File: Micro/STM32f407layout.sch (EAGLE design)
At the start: 68 parts, among them Q1 ASF, Q2 ASV-8, T3 FDN340P, T4 AP1117_LIN_REG

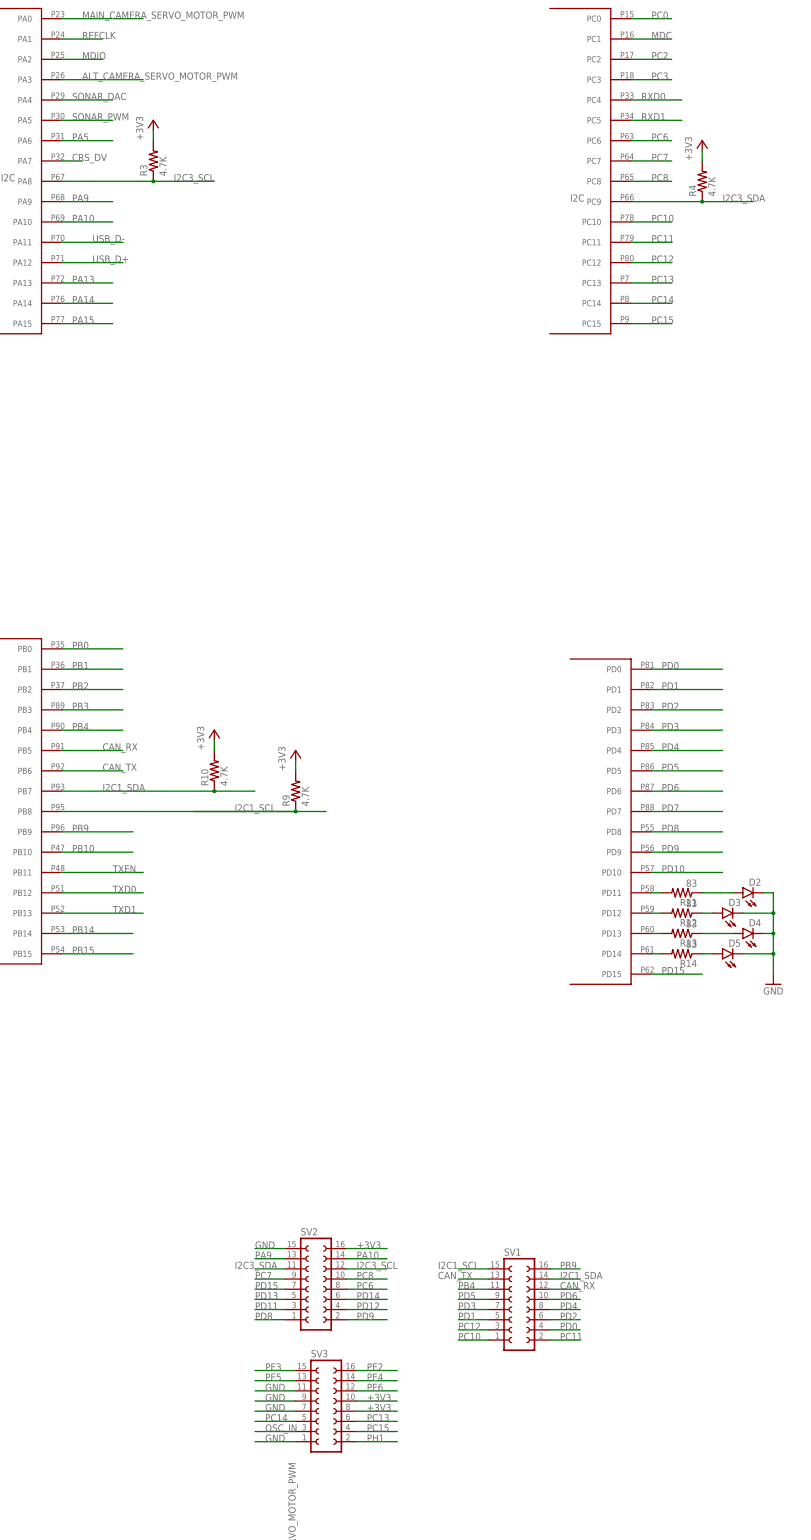
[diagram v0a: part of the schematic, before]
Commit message: Added rough sketch for bottom pinout
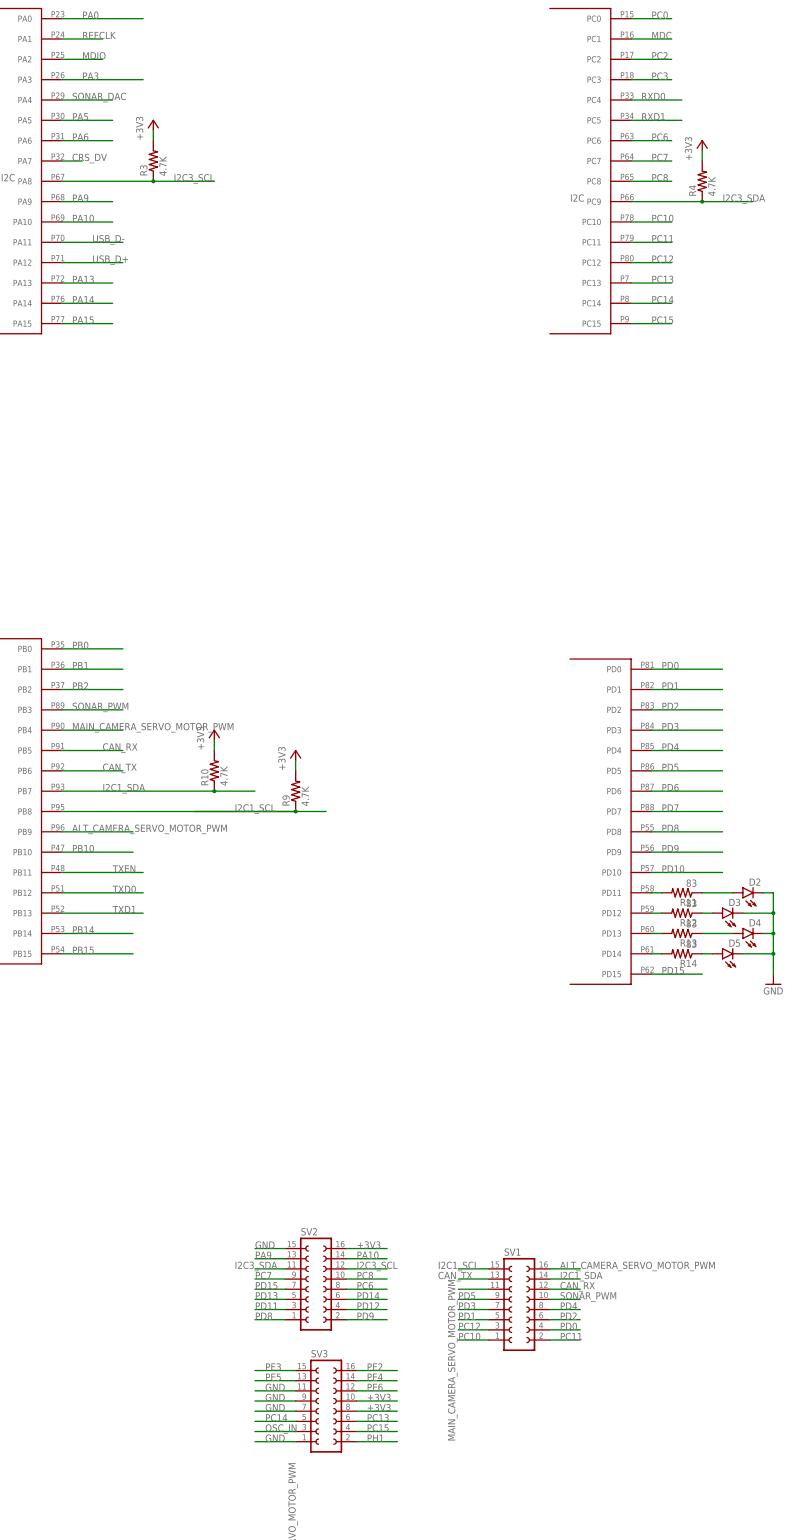
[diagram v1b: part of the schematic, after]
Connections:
- removed net PB3: U$1G$2.PB3
- removed net PB4: SV1.11, U$1G$2.PB4
- removed net PB9: SV1.16, U$1G$2.PB9
- new net PA0: U$1G$1.PA0
- new net PA3: U$1G$1.PA3
- new net PA6: U$1G$1.PA6
- net ALT_CAMERA_SERVO_MOTOR_PWM: now also SV1.16, U$1G$2.PB9; no longer U$1G$1.PA3
- net MAIN_CAMERA_SERVO_MOTOR_PWM: now also SV1.11, U$1G$2.PB4; no longer U$1G$1.PA0
- net PA5: now also U$1G$1.PA5; no longer U$1G$1.PA6
- net PD6: no longer SV1.10
- net SONAR_PWM: now also SV1.10, U$1G$2.PB3; no longer U$1G$1.PA5
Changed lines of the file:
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@@
 <?xml version="1.0" encoding="utf-8"?>
 <!DOCTYPE eagle SYSTEM "eagle.dtd">
-<eagle version="7.4.0">
+<eagle version="7.5.0">
 <drawing>
 <settings>
@@
 <net name="SONAR_PWM" class="0">
 <segment>
-<pinref part="U$1" gate="G$1" pin="PA5"/>
-<wire x1="439.42" y1="485.14" x2="452.12" y2="485.14" width="0.1524" layer="91"/>
-<label x="441.96" y="485.14" size="1.778" layer="95"/>
-</segment>
-<segment>
 <pinref part="SV4" gate="G$1" pin="7"/>
 <wire x1="500.38" y1="104.14" x2="495.3" y2="104.14" width="0.1524" layer="91"/>
 <label x="485.14" y="104.14" size="1.778" layer="95"/>
+</segment>
+<segment>
+<pinref part="SV1" gate="G$1" pin="10"/>
+<wire x1="561.34" y1="190.5" x2="568.96" y2="190.5" width="0.1524" layer="91"/>
+<label x="563.88" y="190.5" size="1.778" layer="95"/>
+</segment>
+<segment>
+<pinref part="U$1" gate="G$2" pin="PB3"/>
+<wire x1="439.42" y1="337.82" x2="454.66" y2="337.82" width="0.1524" layer="91"/>
+<label x="441.96" y="337.82" size="1.778" layer="95"/>
 </segment>
 </net>
@@
 <net name="MAIN_CAMERA_SERVO_MOTOR_PWM" class="0">
 <segment>
-<pinref part="U$1" gate="G$1" pin="PA0"/>
-<wire x1="439.42" y1="510.54" x2="459.74" y2="510.54" width="0.1524" layer="91"/>
-<label x="444.5" y="510.54" size="1.778" layer="95"/>
-</segment>
-<segment>
 <pinref part="SV4" gate="G$1" pin="11"/>
 <wire x1="500.38" y1="109.22" x2="495.3" y2="109.22" width="0.1524" layer="91"/>
 <label x="497.84" y="109.22" size="1.778" layer="95" rot="R90"/>
 </segment>
+<segment>
+<pinref part="U$1" gate="G$2" pin="PB4"/>
+<wire x1="439.42" y1="332.74" x2="454.66" y2="332.74" width="0.1524" layer="91"/>
+<label x="441.96" y="332.74" size="1.778" layer="95"/>
+</segment>
+<segment>
+<pinref part="SV1" gate="G$1" pin="11"/>
+<wire x1="546.1" y1="193.04" x2="538.48" y2="193.04" width="0.1524" layer="91"/>
+<label x="535.94" y="195.58" size="1.778" layer="95" rot="R270"/>
+</segment>
 </net>
 <net name="ALT_CAMERA_SERVO_MOTOR_PWM" class="0">
-<segment>
-<pinref part="U$1" gate="G$1" pin="PA3"/>
-<wire x1="439.42" y1="495.3" x2="459.74" y2="495.3" width="0.1524" layer="91"/>
-<label x="444.5" y="495.3" size="1.778" layer="95"/>
-</segment>
 <segment>
 <pinref part="SV4" gate="G$1" pin="12"/>
 <wire x1="515.62" y1="109.22" x2="523.24" y2="109.22" width="0.1524" layer="91"/>
 <label x="515.62" y="109.22" size="1.778" layer="95"/>
+</segment>
+<segment>
+<pinref part="U$1" gate="G$2" pin="PB9"/>
+<wire x1="439.42" y1="307.34" x2="457.2" y2="307.34" width="0.1524" layer="91"/>
+<label x="441.96" y="307.34" size="1.778" layer="95"/>
+</segment>
+<segment>
+<pinref part="SV1" gate="G$1" pin="16"/>
+<wire x1="561.34" y1="198.12" x2="568.96" y2="198.12" width="0.1524" layer="91"/>
+<label x="563.88" y="198.12" size="1.778" layer="95"/>
 </segment>
 </net>
@@
 </segment>
 </net>
-<net name="PB9" class="0">
-<segment>
-<pinref part="SV1" gate="G$1" pin="16"/>
-<wire x1="561.34" y1="198.12" x2="568.96" y2="198.12" width="0.1524" layer="91"/>
-<label x="563.88" y="198.12" size="1.778" layer="95"/>
-</segment>
-<segment>
-<pinref part="U$1" gate="G$2" pin="PB9"/>
-<wire x1="439.42" y1="307.34" x2="457.2" y2="307.34" width="0.1524" layer="91"/>
-<label x="441.96" y="307.34" size="1.778" layer="95"/>
-</segment>
-</net>
 <net name="PD6" class="0">
-<segment>
-<pinref part="SV1" gate="G$1" pin="10"/>
-<wire x1="561.34" y1="190.5" x2="568.96" y2="190.5" width="0.1524" layer="91"/>
-<label x="563.88" y="190.5" size="1.778" layer="95"/>
-</segment>
 <segment>
 <pinref part="U$1" gate="G$4" pin="PD6"/>
@@
 </segment>
 </net>
-<net name="PB4" class="0">
-<segment>
-<pinref part="SV1" gate="G$1" pin="11"/>
-<wire x1="546.1" y1="193.04" x2="538.48" y2="193.04" width="0.1524" layer="91"/>
-<label x="538.48" y="193.04" size="1.778" layer="95"/>
-</segment>
-<segment>
-<pinref part="U$1" gate="G$2" pin="PB4"/>
-<wire x1="439.42" y1="332.74" x2="454.66" y2="332.74" width="0.1524" layer="91"/>
-<label x="441.96" y="332.74" size="1.778" layer="95"/>
-</segment>
-</net>
 <net name="PA10" class="0">
 <segment>
@@
 </segment>
 </net>
-<net name="PA5" class="0">
+<net name="PA6" class="0">
 <segment>
 <pinref part="U$1" gate="G$1" pin="PA6"/>
@@
 <wire x1="439.42" y1="276.86" x2="457.2" y2="276.86" width="0.1524" layer="91"/>
 <label x="441.96" y="276.86" size="1.778" layer="95"/>
-</segment>
-</net>
-<net name="PB3" class="0">
-<segment>
-<pinref part="U$1" gate="G$2" pin="PB3"/>
-<wire x1="439.42" y1="337.82" x2="454.66" y2="337.82" width="0.1524" layer="91"/>
-<label x="441.96" y="337.82" size="1.778" layer="95"/>
 </segment>
 </net>
@@
 </segment>
 </net>
+<net name="PA5" class="0">
+<segment>
+<pinref part="U$1" gate="G$1" pin="PA5"/>
+<wire x1="439.42" y1="485.14" x2="452.12" y2="485.14" width="0.1524" layer="91"/>
+<label x="441.96" y="485.14" size="1.778" layer="95"/>
+</segment>
+</net>
+<net name="PA0" class="0">
+<segment>
+<pinref part="U$1" gate="G$1" pin="PA0"/>
+<wire x1="439.42" y1="510.54" x2="459.74" y2="510.54" width="0.1524" layer="91"/>
+<label x="444.5" y="510.54" size="1.778" layer="95"/>
+</segment>
+</net>
+<net name="PA3" class="0">
+<segment>
+<pinref part="U$1" gate="G$1" pin="PA3"/>
+<wire x1="439.42" y1="495.3" x2="459.74" y2="495.3" width="0.1524" layer="91"/>
+<label x="444.5" y="495.3" size="1.778" layer="95"/>
+</segment>
+</net>

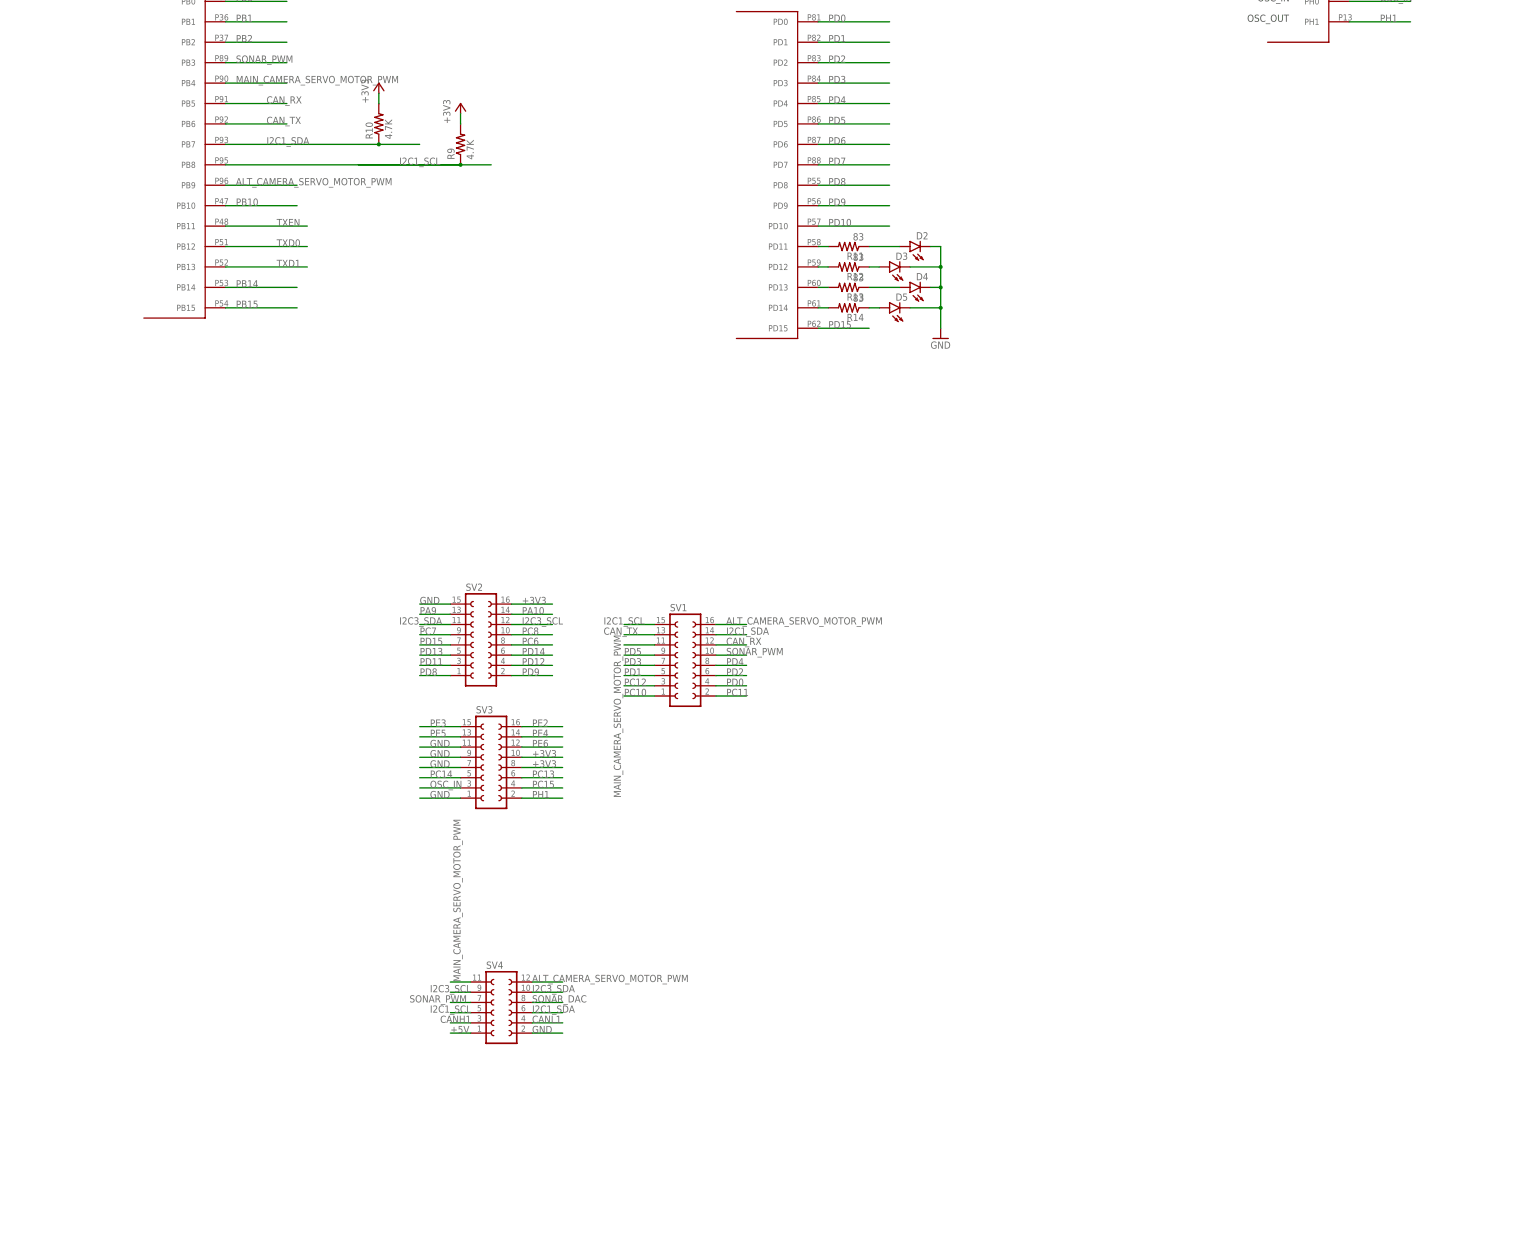
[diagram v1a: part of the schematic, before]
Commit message: added real header pin
Did a rough draft of connections to backplane
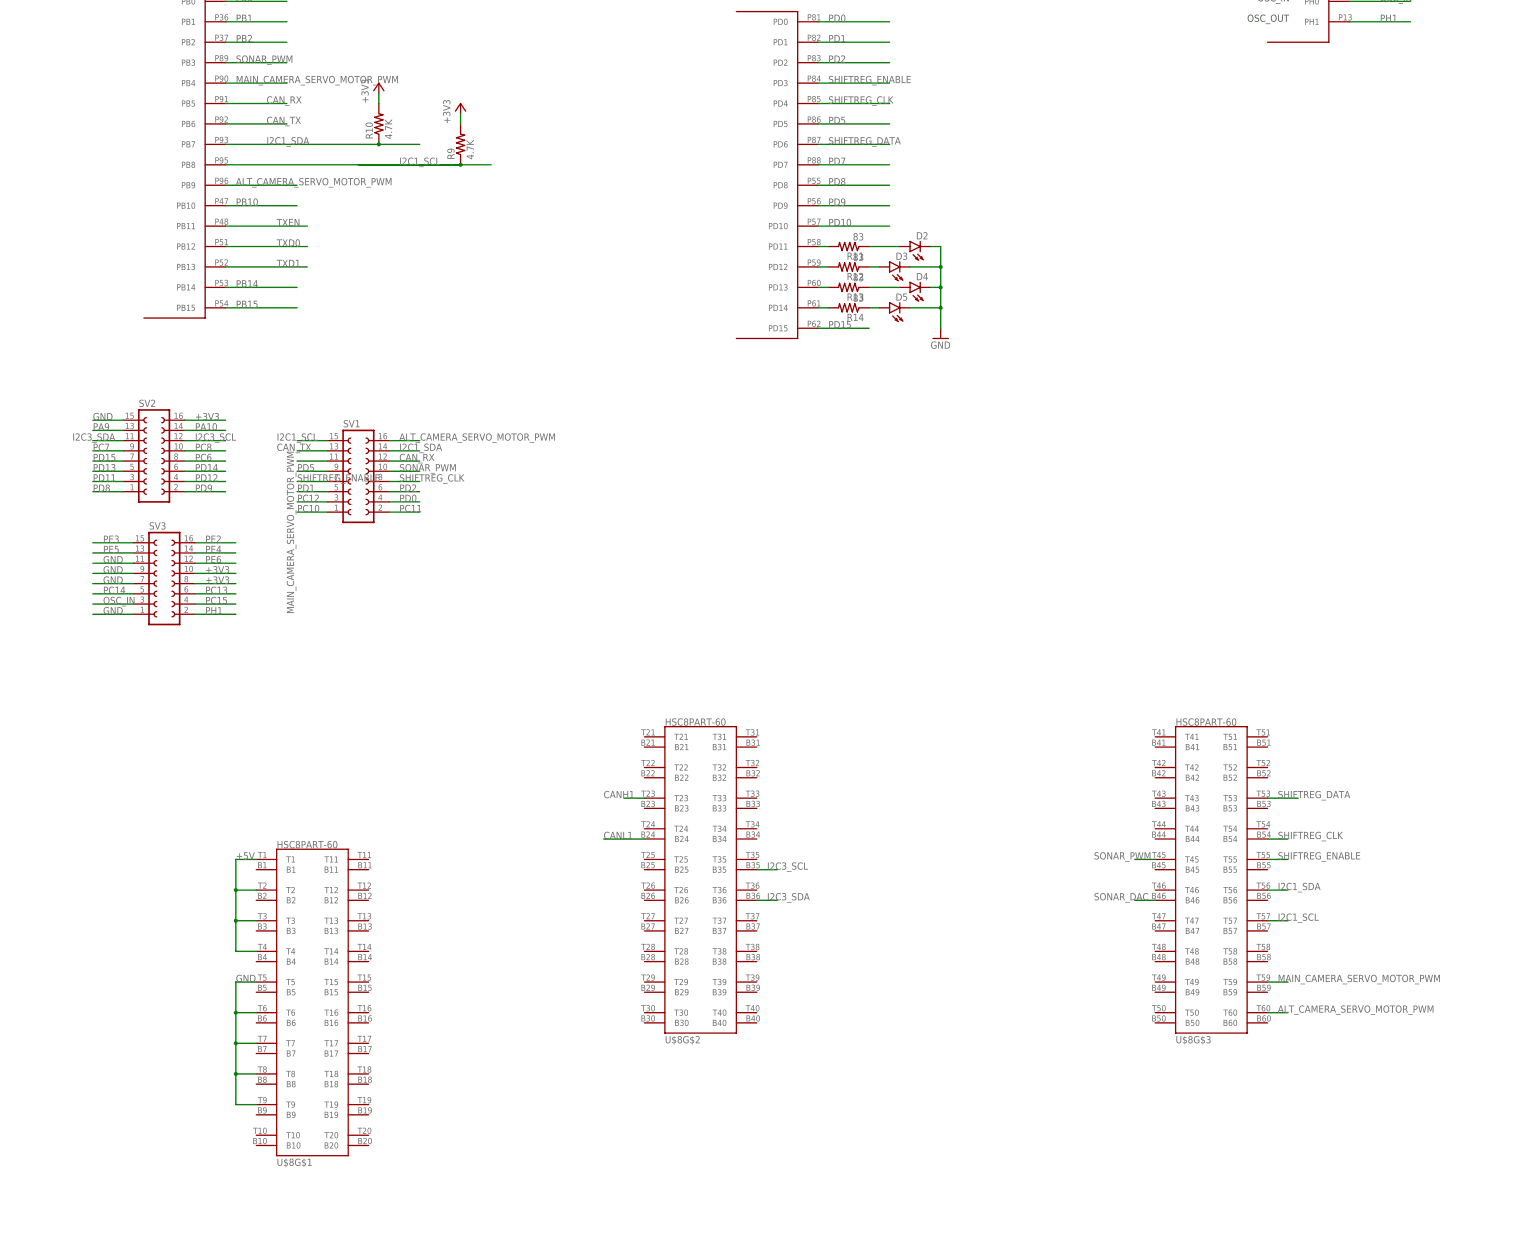
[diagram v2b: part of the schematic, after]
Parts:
- removed SV4: (no value), con-lsta:FE06-2
- added U$8: HSC8PART-60, Connectors:HSC8PART-60
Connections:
- removed net PD3: SV1.7, U$1G$4.PD3
- removed net PD4: SV1.8, U$1G$4.PD4
- removed net PD6: U$1G$4.PD6
- new net SHIFTREG_CLK: SV1.8, U$1G$4.PD4, U$8G$3.B54
- new net SHIFTREG_DATA: U$1G$4.PD6, U$8G$3.T53
- new net SHIFTREG_ENABLE: SV1.7, U$1G$4.PD3, U$8G$3.T55
- net +5V: now also U$8G$1.T1, U$8G$1.T2, U$8G$1.T3, U$8G$1.T4; no longer SV4.1
- net ALT_CAMERA_SERVO_MOTOR_PWM: now also U$8G$3.T60; no longer SV4.12
- net CANH1: now also U$8G$2.T23; no longer SV4.3
- net CANL1: now also U$8G$2.B24; no longer SV4.4
- net GND: now also U$8G$1.T5, U$8G$1.T6, U$8G$1.T7, U$8G$1.T8, U$8G$1.T9; no longer SV4.2
- net I2C1_SCL: now also U$8G$3.T57; no longer SV4.5
- net I2C1_SDA: now also U$8G$3.T56; no longer SV4.6
- net I2C3_SCL: now also U$8G$2.B35; no longer SV4.9
- net I2C3_SDA: now also U$8G$2.B36; no longer SV4.10
- net MAIN_CAMERA_SERVO_MOTOR_PWM: now also U$8G$3.T59; no longer SV4.11
- net SONAR_DAC: now also U$8G$3.B46; no longer SV4.8
- net SONAR_PWM: now also U$8G$3.T45; no longer SV4.7
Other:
- moved on the sheet: SV1, SV2, SV3
